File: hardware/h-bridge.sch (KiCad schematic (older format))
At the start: 78 parts, among them M1 MOUNTING_HOLE, M2 MOUNTING_HOLE, M3 MOUNTING_HOLE, M4 MOUNTING_HOLE, M5 MOUNTING_HOLE, M6 MOUNTING_HOLE, P10 CONN_01_BRK, P11 CONN_01_M+, P12 CONN_01_M-, P8 CONN_01_V+, P9 CONN_01_V-, Q10 PSMN021-100, Q3 IRFP4468, Q4 PSMN021-100, Q5 IRFP4468, Q6 IRFP4468, Q7 IRFP4468, Q8 IRFP4468, Q9 IRFP4468, U16 Si8045AA, U17 MIC4127, U18 MIC4127, U19 LM5102, U20 Si8045AA, U21 LM5102

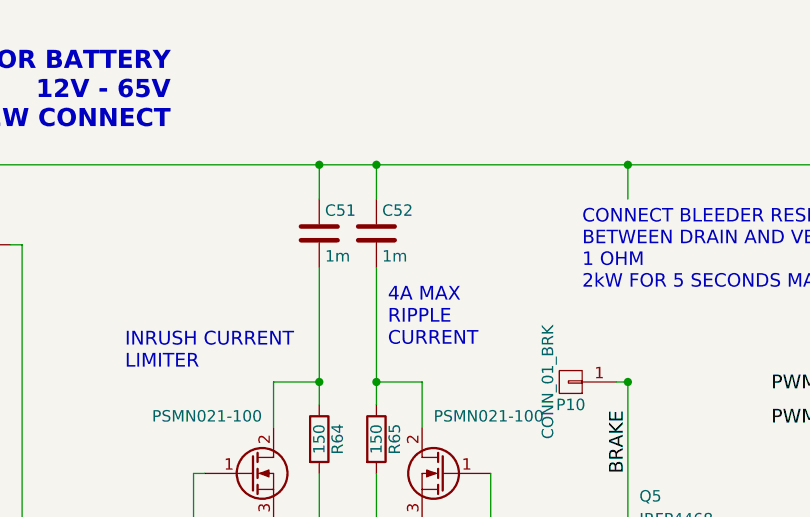
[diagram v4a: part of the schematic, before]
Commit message: High amp routes, sensors
- Adjusted high current routing to improve clearances. Recommend
  3mm high busbar to compensate for reduced busbar width to 2mm.
- Shrank TO-247 pads by 1mm (lengthwise) to improve busbar clearance.
- Removed unecessary buffers / SAR ADC drive circuits from low-bandwidth
  sensors.
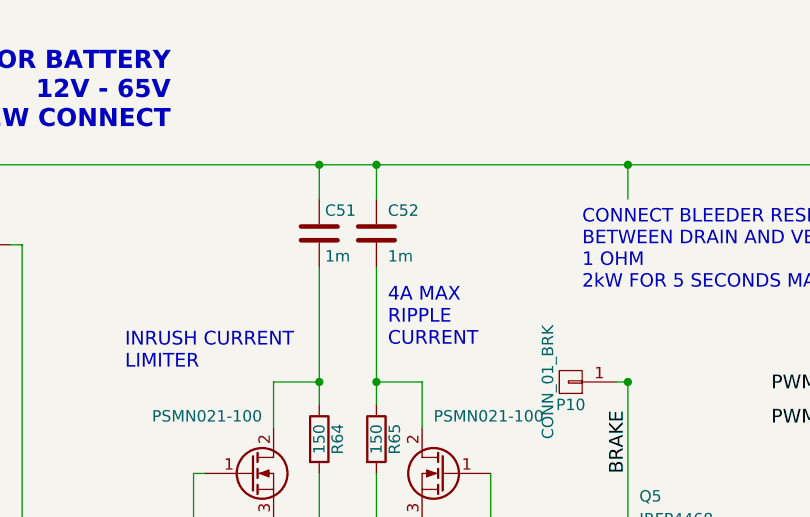
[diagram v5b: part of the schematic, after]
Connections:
- net VBUS: now also C52.2; no longer C52.1
- net at Q4.2 (D), R65.1: now also C52.1; no longer C52.2
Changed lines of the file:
@@
 $EndComp
 $Comp
-L GNDPWR #PWR091
+L GNDPWR #PWR083
 U 1 1 5975827F
 P 7800 3600
-F 0 "#PWR091" H 7800 3400 50  0001 C CNN
+F 0 "#PWR083" H 7800 3400 50  0001 C CNN
 F 1 "GNDPWR" H 7800 3470 50  0000 C CNN
 F 2 "" H 7800 3550 50  0000 C CNN
@@
 $EndComp
 $Comp
-L GNDPWR #PWR092
+L GNDPWR #PWR084
 U 1 1 59959CCF
 P 5200 1950
-F 0 "#PWR092" H 5200 1750 50  0001 C CNN
+F 0 "#PWR084" H 5200 1750 50  0001 C CNN
 F 1 "GNDPWR" H 5200 1820 50  0000 C CNN
 F 2 "" H 5200 1900 50  0000 C CNN
@@
 $EndComp
 $Comp
-L +12V_ISO #PWR093
+L +12V_ISO #PWR085
 U 1 1 5995F515
 P 5450 1550
-F 0 "#PWR093" H 5450 1400 50  0001 C CNN
+F 0 "#PWR085" H 5450 1400 50  0001 C CNN
 F 1 "+12V_ISO" H 5450 1690 50  0000 C CNN
 F 2 "" H 5450 1550 50  0000 C CNN
@@
 $EndComp
 $Comp
-L GNDPWR #PWR094
+L GNDPWR #PWR086
 U 1 1 5998917B
 P 10300 1950
-F 0 "#PWR094" H 10300 1750 50  0001 C CNN
+F 0 "#PWR086" H 10300 1750 50  0001 C CNN
 F 1 "GNDPWR" H 10300 1820 50  0000 C CNN
 F 2 "" H 10300 1900 50  0000 C CNN
@@
 $EndComp
 $Comp
-L +12V_ISO #PWR095
+L +12V_ISO #PWR087
 U 1 1 59989187
 P 10050 1550
-F 0 "#PWR095" H 10050 1400 50  0001 C CNN
+F 0 "#PWR087" H 10050 1400 50  0001 C CNN
 F 1 "+12V_ISO" H 10050 1690 50  0000 C CNN
 F 2 "" H 10050 1550 50  0000 C CNN
@@
 $EndComp
 $Comp
-L GNDPWR #PWR096
+L GNDPWR #PWR088
 U 1 1 599891AB
 P 9150 2950
-F 0 "#PWR096" H 9150 2750 50  0001 C CNN
+F 0 "#PWR088" H 9150 2750 50  0001 C CNN
 F 1 "GNDPWR" H 9250 2800 50  0000 C CNN
 F 2 "" H 9150 2900 50  0000 C CNN
@@
 U 1 1 5999779C
 P 2650 1500
-F 0 "C52" H 2675 1600 50  0000 L CNN
-F 1 "1m" H 2675 1400 50  0000 L CNN
+F 0 "C52" H 2700 1400 50  0000 L CNN
+F 1 "1m" H 2700 1600 50  0000 L CNN
 F 2 "2kwMotorController:Cap_Horizontal_D18_L36" H 2688 1350 50  0001 C CNN
 F 3 "" H 2650 1500 50  0000 C CNN
 	1    2650 1500
-	1    0    0    -1
-$EndComp
-$Comp
-L GNDPWR #PWR097
+	1    0    0    1
+$EndComp
+$Comp
+L GNDPWR #PWR089
 U 1 1 59967530
 P 6350 2950
-F 0 "#PWR097" H 6350 2750 50  0001 C CNN
+F 0 "#PWR089" H 6350 2750 50  0001 C CNN
 F 1 "GNDPWR" H 6450 2800 50  0000 C CNN
 F 2 "" H 6350 2900 50  0000 C CNN
@@
 H-BRIDGE\n90A MAX\n20 kHz
 $Comp
-L GNDPWR #PWR098
+L GNDPWR #PWR090
 U 1 1 599BCA83
 P 2400 3600
-F 0 "#PWR098" H 2400 3400 50  0001 C CNN
+F 0 "#PWR090" H 2400 3400 50  0001 C CNN
 F 1 "GNDPWR" H 2400 3470 50  0000 C CNN
 F 2 "" H 2400 3550 50  0000 C CNN
@@
 $EndComp
 $Comp
-L +3.3V #PWR099
+L +3.3V #PWR091
 U 1 1 599D3CAE
 P 8100 4400
-F 0 "#PWR099" H 8100 4250 50  0001 C CNN
+F 0 "#PWR091" H 8100 4250 50  0001 C CNN
 F 1 "+3.3V" H 8100 4540 50  0000 C CNN
 F 2 "" H 8100 4400 50  0000 C CNN
@@
 $EndComp
 $Comp
-L GND #PWR0100
+L GND #PWR092
 U 1 1 599D3CC0
 P 7900 4750
-F 0 "#PWR0100" H 7900 4500 50  0001 C CNN
+F 0 "#PWR092" H 7900 4500 50  0001 C CNN
 F 1 "GND" H 7900 4600 50  0000 C CNN
 F 2 "" H 7900 4750 50  0000 C CNN
@@
 $EndComp
 $Comp
-L +5V_ISO #PWR0101
+L +5V_ISO #PWR093
 U 1 1 599D3CD5
 P 9200 4400
-F 0 "#PWR0101" H 9200 4250 50  0001 C CNN
+F 0 "#PWR093" H 9200 4250 50  0001 C CNN
 F 1 "+5V_ISO" H 9200 4540 50  0000 C CNN
 F 2 "" H 9200 4400 50  0000 C CNN
@@
 $EndComp
 $Comp
-L GNDPWR #PWR0102
+L GNDPWR #PWR094
 U 1 1 599D3CF4
 P 9400 4750
-F 0 "#PWR0102" H 9400 4550 50  0001 C CNN
+F 0 "#PWR094" H 9400 4550 50  0001 C CNN
 F 1 "GNDPWR" H 9400 4620 50  0000 C CNN
 F 2 "" H 9400 4700 50  0000 C CNN
@@
 $EndComp
 $Comp
-L +12V_ISO #PWR0103
+L +12V_ISO #PWR095
 U 1 1 59A0BCFD
 P 6150 3850
-F 0 "#PWR0103" H 6150 3700 50  0001 C CNN
+F 0 "#PWR095" H 6150 3700 50  0001 C CNN
 F 1 "+12V_ISO" H 6150 3990 50  0000 C CNN
 F 2 "" H 6150 3850 50  0000 C CNN
@@
 $EndComp
 $Comp
-L GNDPWR #PWR0104
+L GNDPWR #PWR096
 U 1 1 59A194F2
 P 5450 3600
-F 0 "#PWR0104" H 5450 3400 50  0001 C CNN
+F 0 "#PWR096" H 5450 3400 50  0001 C CNN
 F 1 "GNDPWR" H 5450 3470 50  0000 C CNN
 F 2 "" H 5450 3550 50  0000 C CNN
@@
 $EndComp
 $Comp
-L GNDPWR #PWR0105
+L GNDPWR #PWR097
 U 1 1 59A199E4
 P 10050 3600
-F 0 "#PWR0105" H 10050 3400 50  0001 C CNN
+F 0 "#PWR097" H 10050 3400 50  0001 C CNN
 F 1 "GNDPWR" H 10050 3470 50  0000 C CNN
 F 2 "" H 10050 3550 50  0000 C CNN
@@
 $EndComp
 $Comp
-L GND #PWR0106
+L GND #PWR098
 U 1 1 59A2238F
 P 8100 5950
-F 0 "#PWR0106" H 8100 5700 50  0001 C CNN
+F 0 "#PWR098" H 8100 5700 50  0001 C CNN
 F 1 "GND" H 8100 5800 50  0000 C CNN
 F 2 "" H 8100 5950 50  0000 C CNN
@@
 $EndComp
 $Comp
-L GNDPWR #PWR0107
+L GNDPWR #PWR099
 U 1 1 59A24543
 P 9200 6000
-F 0 "#PWR0107" H 9200 5800 50  0001 C CNN
+F 0 "#PWR099" H 9200 5800 50  0001 C CNN
 F 1 "GNDPWR" H 9200 5870 50  0000 C CNN
 F 2 "" H 9200 5950 50  0000 C CNN
@@
 VBUS
 $Comp
-L GNDMBAT #PWR0108
+L GNDMBAT #PWR0100
 U 1 1 59C09326
 P 1000 3600
-F 0 "#PWR0108" H 1000 3350 50  0001 C CNN
+F 0 "#PWR0100" H 1000 3350 50  0001 C CNN
 F 1 "GNDMBAT" H 1000 3450 50  0000 C CNN
 F 2 "" H 1000 3600 50  0000 C CNN
@@
 $EndComp
 $Comp
-L +12V_ISO #PWR0109
+L +12V_ISO #PWR0101
 U 1 1 59CA0DB7
 P 6150 4700
-F 0 "#PWR0109" H 6150 4550 50  0001 C CNN
+F 0 "#PWR0101" H 6150 4550 50  0001 C CNN
 F 1 "+12V_ISO" H 6150 4840 50  0000 C CNN
 F 2 "" H 6150 4700 50  0000 C CNN
@@
 $EndComp
 $Comp
-L GNDPWR #PWR0110
+L GNDPWR #PWR0102
 U 1 1 59BAB965
 P 2900 7250
-F 0 "#PWR0110" H 2900 7050 50  0001 C CNN
+F 0 "#PWR0102" H 2900 7050 50  0001 C CNN
 F 1 "GNDPWR" H 2900 7120 50  0000 C CNN
 F 2 "" H 2900 7200 50  0000 C CNN
@@
 $EndComp
 $Comp
-L GND #PWR0111
+L GND #PWR0103
 U 1 1 59BAD34A
 P 1750 7250
-F 0 "#PWR0111" H 1750 7000 50  0001 C CNN
+F 0 "#PWR0103" H 1750 7000 50  0001 C CNN
 F 1 "GND" H 1750 7100 50  0000 C CNN
 F 2 "" H 1750 7250 50  0000 C CNN
@@
 $EndComp
 $Comp
-L +3.3V #PWR0112
+L +3.3V #PWR0104
 U 1 1 59BAFE13
 P 1800 5700
-F 0 "#PWR0112" H 1800 5550 50  0001 C CNN
+F 0 "#PWR0104" H 1800 5550 50  0001 C CNN
 F 1 "+3.3V" H 1800 5840 50  0000 C CNN
 F 2 "" H 1800 5700 50  0000 C CNN
@@
 $EndComp
 $Comp
-L GND #PWR0113
+L GND #PWR0105
 U 1 1 59BAFE19
 P 1600 6050
-F 0 "#PWR0113" H 1600 5800 50  0001 C CNN
+F 0 "#PWR0105" H 1600 5800 50  0001 C CNN
 F 1 "GND" H 1600 5900 50  0000 C CNN
 F 2 "" H 1600 6050 50  0000 C CNN
@@
 $EndComp
 $Comp
-L +5V_ISO #PWR0114
+L +5V_ISO #PWR0106
 U 1 1 59BB121B
 P 2900 5700
-F 0 "#PWR0114" H 2900 5550 50  0001 C CNN
+F 0 "#PWR0106" H 2900 5550 50  0001 C CNN
 F 1 "+5V_ISO" H 2900 5840 50  0000 C CNN
 F 2 "" H 2900 5700 50  0000 C CNN
@@
 $EndComp
 $Comp
-L GNDPWR #PWR0115
+L GNDPWR #PWR0107
 U 1 1 59BB1221
 P 3100 6050
-F 0 "#PWR0115" H 3100 5850 50  0001 C CNN
+F 0 "#PWR0107" H 3100 5850 50  0001 C CNN
 F 1 "GNDPWR" H 3100 5920 50  0000 C CNN
 F 2 "" H 3100 6000 50  0000 C CNN
@@
 	9400 1600 9400 1750
 $Comp
-L GNDPWR #PWR0116
+L GNDPWR #PWR0108
 U 1 1 59BF5AC7
 P 9400 1750
-F 0 "#PWR0116" H 9400 1550 50  0001 C CNN
+F 0 "#PWR0108" H 9400 1550 50  0001 C CNN
 F 1 "GNDPWR" H 9400 1620 50  0000 C CNN
 F 2 "" H 9400 1700 50  0000 C CNN
@@
 	6800 1600 6800 1750
 $Comp
-L GNDPWR #PWR0117
+L GNDPWR #PWR0109
 U 1 1 59BF8AEF
 P 6800 1750
-F 0 "#PWR0117" H 6800 1550 50  0001 C CNN
+F 0 "#PWR0109" H 6800 1550 50  0001 C CNN
 F 1 "GNDPWR" H 6800 1620 50  0000 C CNN
 F 2 "" H 6800 1700 50  0000 C CNN

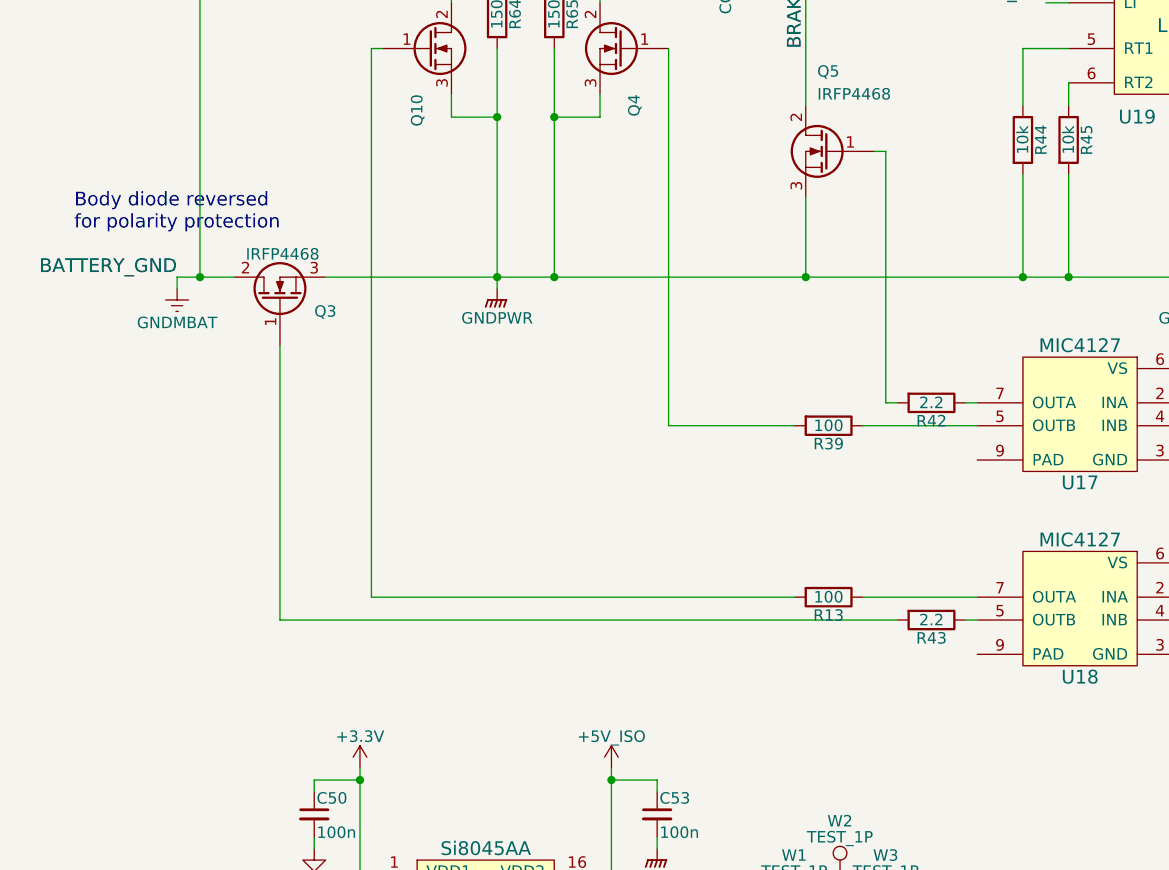
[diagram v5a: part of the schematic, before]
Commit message: Draft layout of controller section
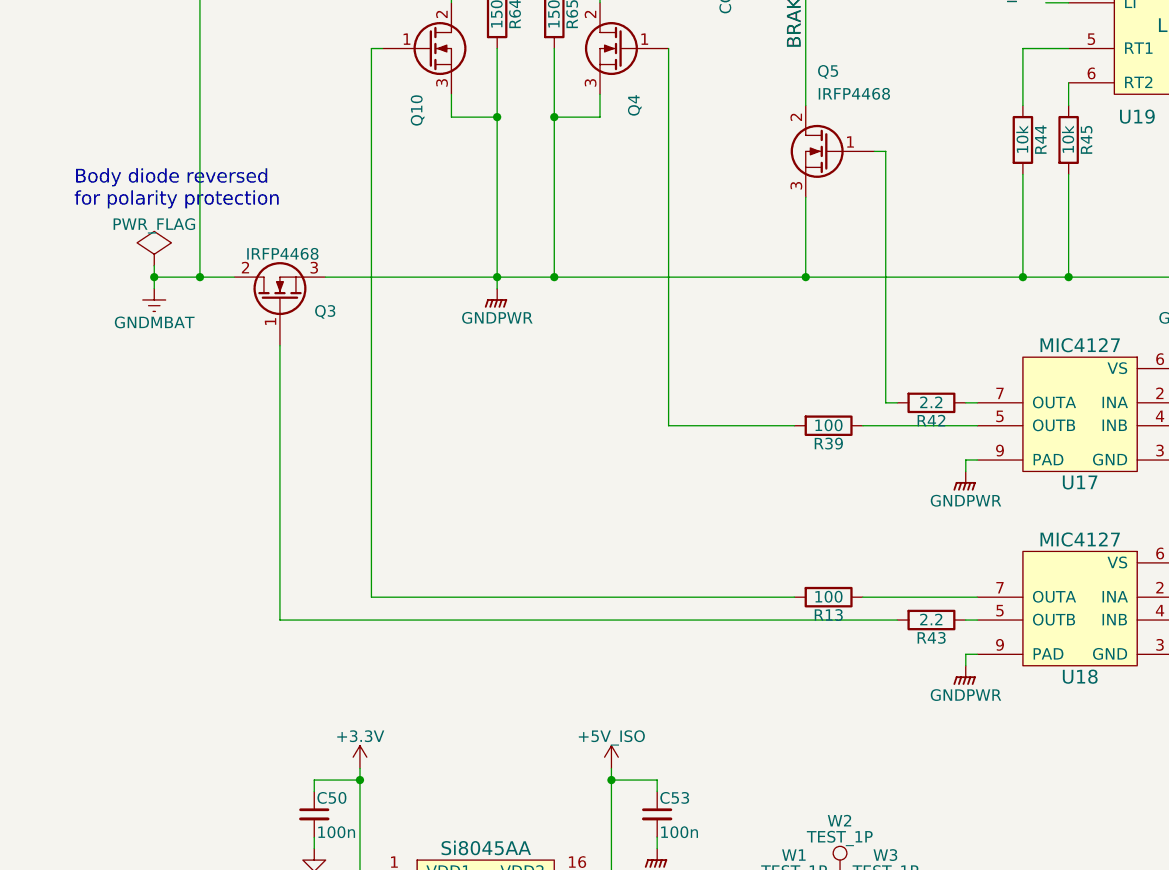
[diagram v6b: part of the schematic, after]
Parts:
- C61, C62, C64, C65: footprint Capacitors_SMD:C_1206 -> Capacitors_SMD:C_0603
- Q10, Q4: footprint TO_SOT_Packages_SMD:SOT-669_LFPAK_ThermalVias-1 -> 2kwMotorController:SOT-669_LFPAK_ThermalVias-1
- U17, U18: footprint Housings_SOIC:SOIC-8_3.9x4.9mm_Pitch1.27mm -> Housings_SOIC:SOIC-8-1EP_3.9x4.9mm_Pitch1.27mm
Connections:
- net GNDPWR: now also U17.9 (PAD), U18.9 (PAD)
